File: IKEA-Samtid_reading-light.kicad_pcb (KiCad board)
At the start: 2 copper layers, 21 x 100 mm, 30 parts, among them IC1 ATTINY25-S, P1 CONN_2, U1 MCP1804-SOT23-5, U2 PT4115-SOT89-5

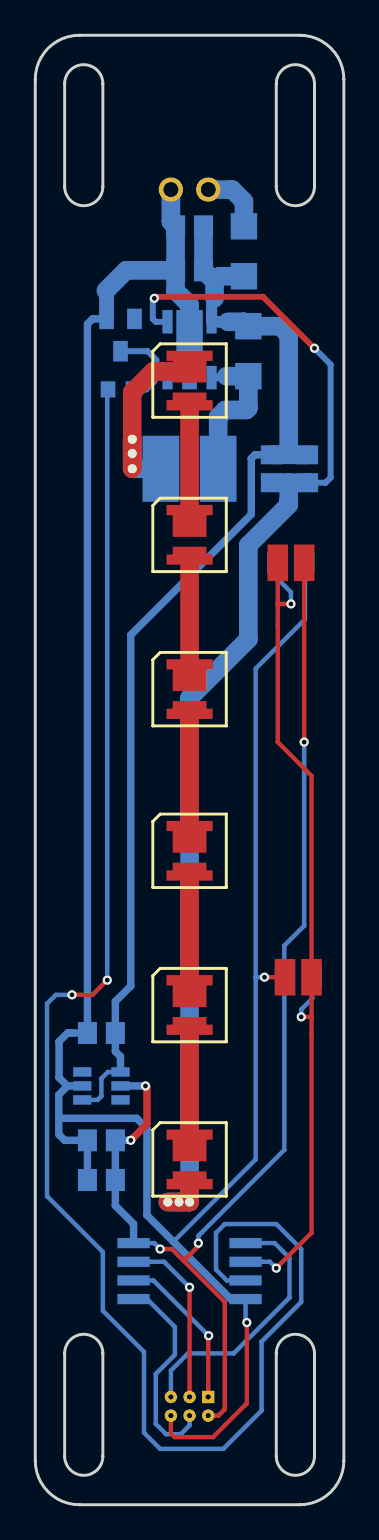
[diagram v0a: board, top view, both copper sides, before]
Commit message: Routing + copper pour.
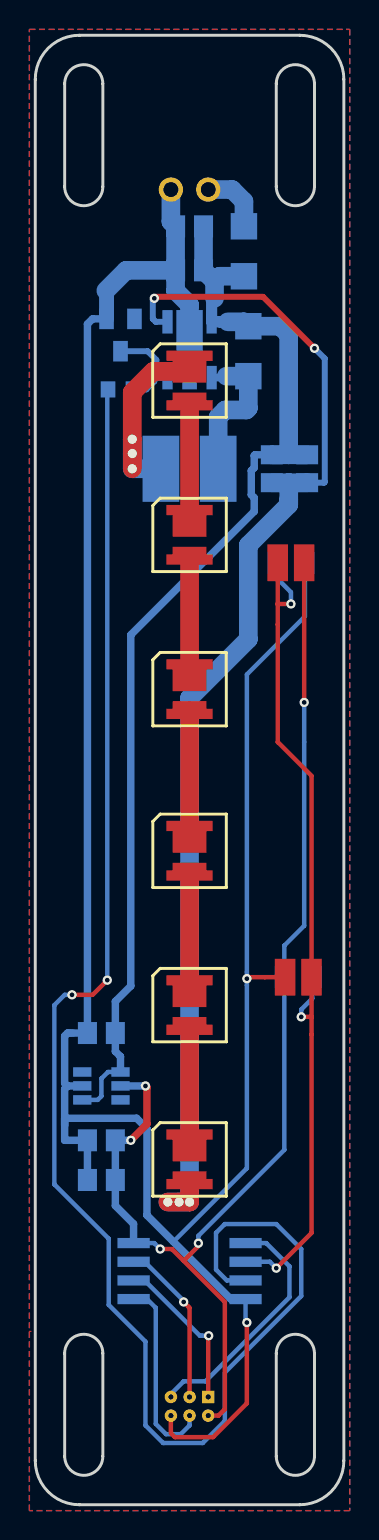
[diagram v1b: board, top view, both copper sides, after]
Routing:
- net /DIM: track 110.1 -> 107.6 mm
- net /RESET: track 18.0 -> 16.7 mm
- net /MOSI: track 14.2 -> 13.2 mm
- net /SCK: track 12.0 -> 11.2 mm
- added copper zone on B.Cu, net GND
- added copper zone on F.Cu, net GNDPWR

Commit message: Back to 100mil AVR_ISP header + layout tweaks.
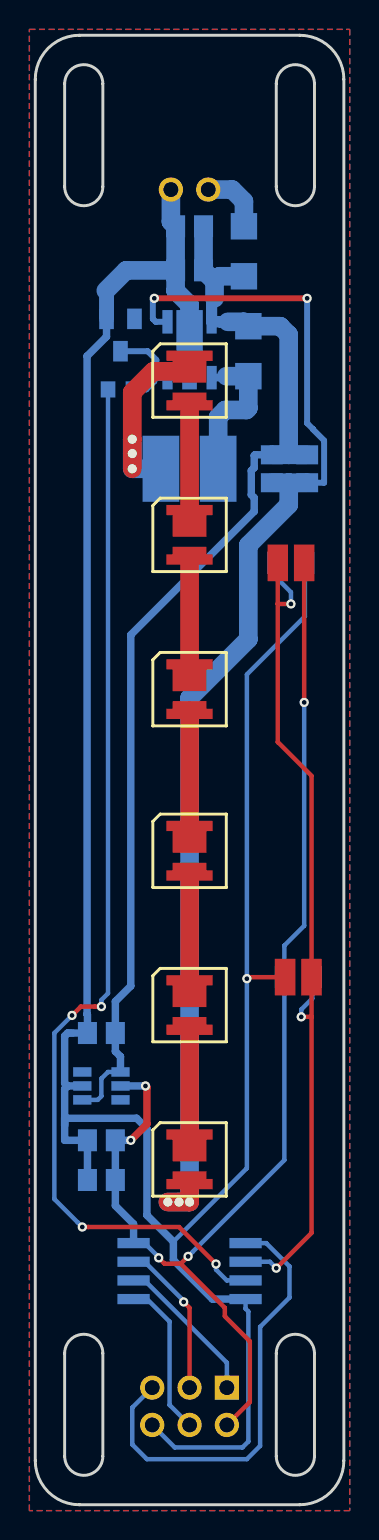
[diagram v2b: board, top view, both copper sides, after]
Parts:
- JP1: footprint my_parts:MADW__PIN_ARRAY_3x2_1.27mm -> my_parts:MADW__PIN_ARRAY_3x2_2.54mm
- turned JP1 to 0 degrees
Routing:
- net /DIM: track 107.6 -> 73.0 mm, vias 2 -> 4
- net /RESET: track 16.7 -> 30.6 mm
- net GND: track 101.5 -> 104.8 mm, vias 2 -> 1
- net /MOSI: track 13.2 -> 11.3 mm
- net /CSN: track 84.5 -> 86.0 mm
- net +5V: track 81.8 -> 83.0 mm
- net /SCK: track 11.2 -> 10.6 mm
- net GNDPWR: track 70.0 -> 69.4 mm
- net /MISO: track 10.8 -> 10.4 mm, vias 1 -> 0

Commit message: 7mm --> 12mm slots (for 10mm tape) + shoved stuff around a bit.
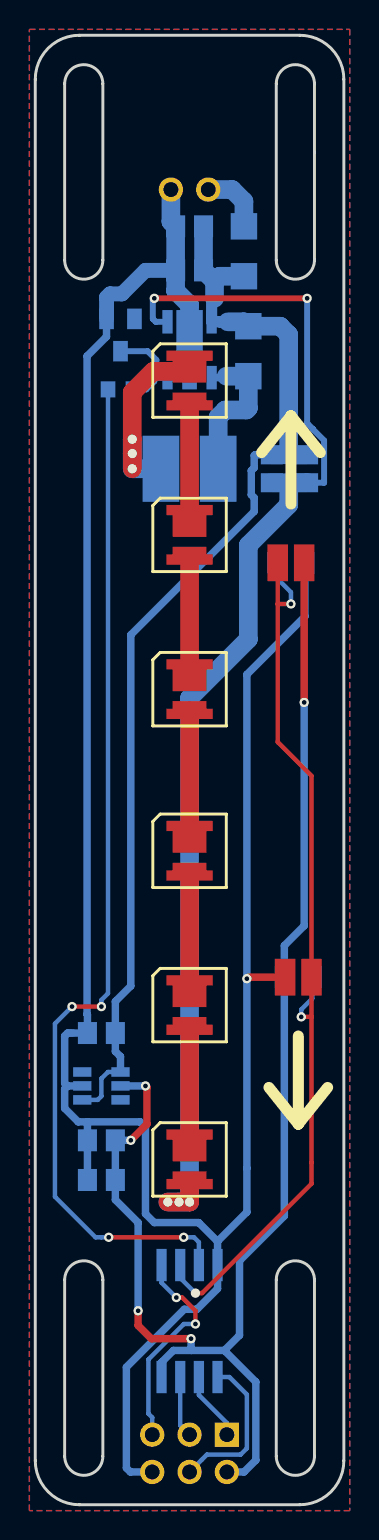
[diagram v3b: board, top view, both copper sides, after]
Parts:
- moved IC1 3.40 mm to (71.0, 126.0), turned to 0 degrees
- moved JP1 3.20 mm to (71.0, 135.0)
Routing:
- net /RESET: track 30.6 -> 14.6 mm, vias 0 -> 2
- net +5V: track 83.0 -> 97.1 mm
- net /SCK: track 10.6 -> 4.18 mm, vias 1 -> 0
- net /MISO: track 10.4 -> 4.71 mm
- net GND: track 104.8 -> 99.8 mm
- net /FSEN: track 60.0 -> 64.3 mm
- net /DIM: track 73.0 -> 70.2 mm
- net /MOSI: track 11.3 -> 10.7 mm
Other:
- outline, holes or cut-outs redrawn

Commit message: Tweaks.
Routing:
- net +24V: track 76.8 -> 79.7 mm

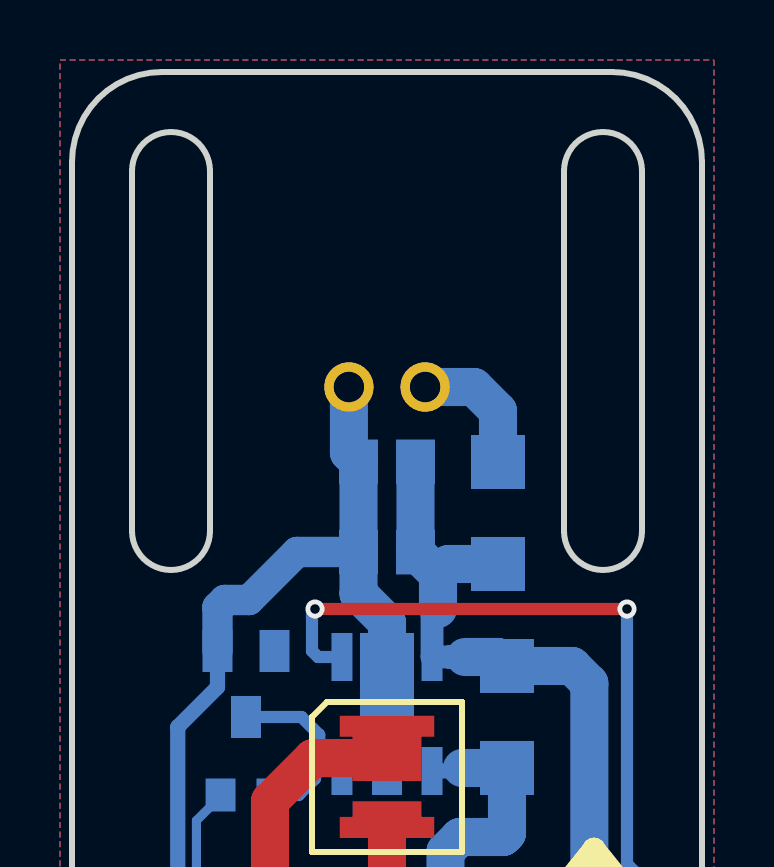
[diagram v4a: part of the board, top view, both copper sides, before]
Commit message: Added slots for zip-ties.
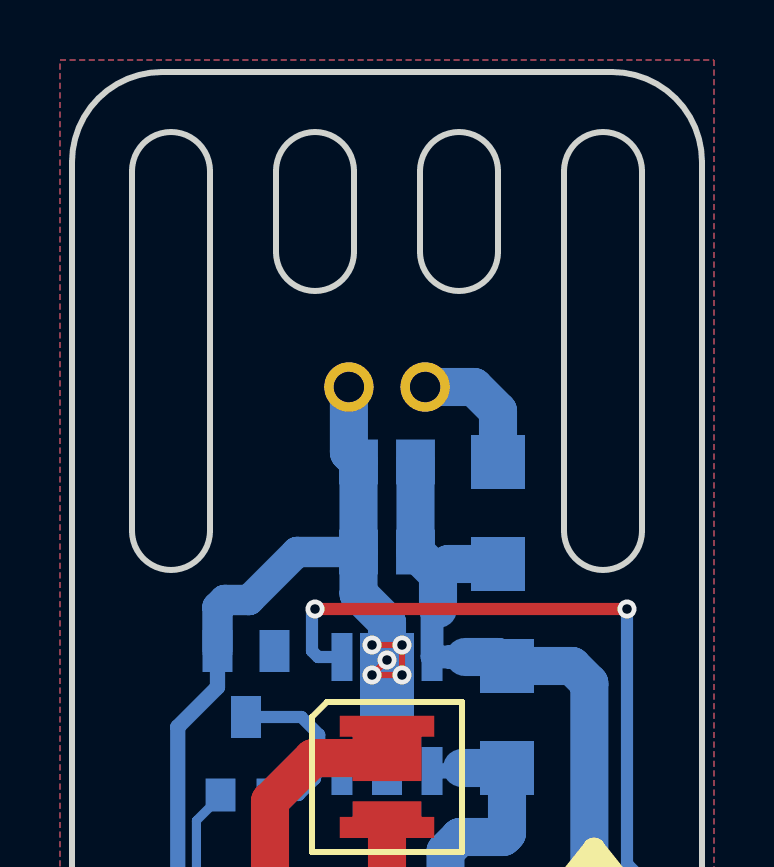
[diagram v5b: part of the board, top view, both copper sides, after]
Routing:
- net GNDPWR: track 69.1 -> 75.9 mm, vias 0 -> 5
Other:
- outline, holes or cut-outs redrawn

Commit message: Shoved parts around a bit. Visually more pleasing now.
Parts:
- moved R_CS1 8.02 mm to (78.5, 60.0)
- moved R_CS2 8.02 mm to (76.1, 60.0)
- moved DS2 1.50 mm to (73.5, 60.0)
- moved DZ1 1.30 mm to (65.0, 58.9)
- moved R2 1.30 mm to (65.0, 62.6)
- moved U2 1.30 mm to (69.7, 59.9)
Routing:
- net +24V: track 79.7 -> 86.8 mm
- net GNDPWR: track 75.9 -> 70.9 mm
- net /SW: track 10.5 -> 9.31 mm
- net /DIM: track 70.5 -> 71.1 mm
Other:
- board text added: "2014 - blog.spitzenpfeil.org Reading-light I**A S*mt*d V0.10.a"
- board text removed: "2014 - blog.spitzenpfeil.org Reading-light I**A S*mt*d"

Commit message: R_FSx 1M --> 10M.
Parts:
- R_FS1, R_FS2: value 1M -> 10M
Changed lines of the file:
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@@
   )
   (setup
-    (last_trace_width 1.27)
+    (last_trace_width 0.2032)
     (user_trace_width 0.2032)
     (user_trace_width 0.3048)
@@
     (pad_to_mask_clearance 0)
     (aux_axis_origin 0 0)
-    (visible_elements 7FFFBF7F)
+    (visible_elements 7FFFBFFF)
     (pcbplotparams
       (layerselection 352092161)
@@
       (effects (font (size 1 1) (thickness 0.2)) (justify mirror))
     )
-    (fp_text value 1M (at 0 -1.9) (layer B.SilkS) hide
+    (fp_text value 10M (at 0 -1.9) (layer B.SilkS) hide
       (effects (font (size 1 1) (thickness 0.2)) (justify mirror))
     )
@@
       (effects (font (size 1 1) (thickness 0.2)) (justify mirror))
     )
-    (fp_text value 1M (at 0 -1.9) (layer B.SilkS) hide
-      (effects (font (size 1 1) (thickness 0.2)) (justify mirror))
-    )
+    (fp_text value 10M (at 0 -1.9) (layer B.SilkS) hide
+      (effects (font (size 1 1) (thickness 0.2)) (justify mirror))
+    )

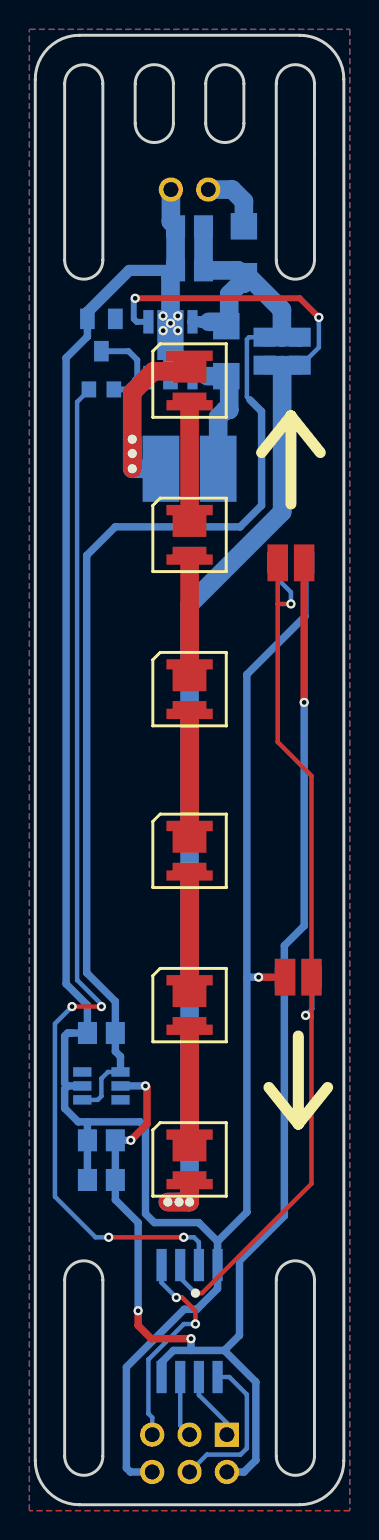
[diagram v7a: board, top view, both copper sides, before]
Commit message: Striving for more horizontal symmetry.
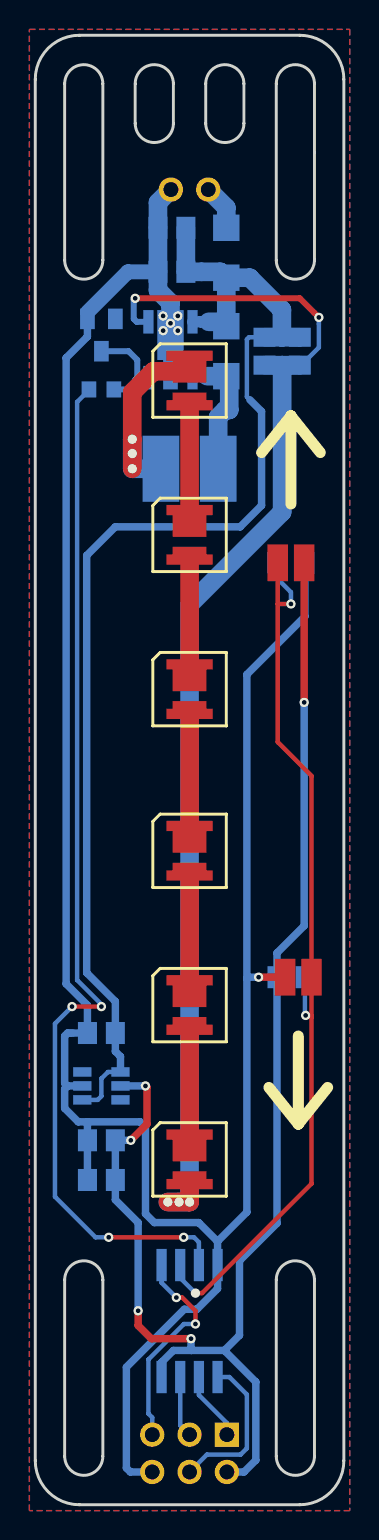
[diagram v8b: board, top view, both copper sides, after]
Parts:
- moved C1 1.20 mm to (69.8, 51.6)
- moved C5 1.20 mm to (69.8, 54.6)
- moved DS1 1.20 mm to (73.5, 53.3)
- moved R_FS1 0.50 mm to (77.9, 102.6)
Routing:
- net Net-(DS1-Pad1): track 4.46 -> 3.11 mm
- net GNDPWR: track 70.9 -> 70.1 mm
